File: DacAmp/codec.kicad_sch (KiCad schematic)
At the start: 0 parts

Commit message: add usb + codec
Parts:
- added C1, C8: 10u, Capacitor_SMD:C_0805_2012Metric_Pad1.18x1.45mm_HandSolder, symbol Device:C
- added C10, C9: 20p, Capacitor_SMD:C_0402_1005Metric_Pad0.74x0.62mm_HandSolder, symbol Device:C
- added C3, C4, C5: 1u, Capacitor_SMD:C_0402_1005Metric_Pad0.74x0.62mm_HandSolder, symbol Device:C
- added C6, C7: 1u, Capacitor_SMD:C_0402_1005Metric_Pad0.74x0.62mm_HandSolder, symbol Device:C_Small
- added R1: 1k5, Resistor_SMD:R_0402_1005Metric_Pad0.72x0.64mm_HandSolder, symbol Device:R_US
- added R3, R4: 22R, Resistor_SMD:R_0402_1005Metric_Pad0.72x0.64mm_HandSolder, symbol Device:R_US
- added R5, R6: 1k5, Resistor_SMD:R_0402_1005Metric_Pad0.72x0.64mm_HandSolder, symbol Device:R_Small_US
- added R7: 1M, Resistor_SMD:R_0402_1005Metric_Pad0.72x0.64mm_HandSolder, symbol Device:R_US
- added U1: PCM2906C, Package_SO:SSOP-28_5.3x10.2mm_P0.65mm, symbol Audio:PCM2902
- added Y1: 12MHz, ABM8:XTAL_ABM8-12.000MHZ-12-B1U-T, symbol Device:Crystal_GND24
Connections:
- new net 3V7: C1.1, U1.10 (VCCCI)
- new net CONN_D+: R1.2, R3.1
- new net CONN_D-: R4.1
- new net GND: C1.2, C10.2, C3.2, C4.2, C5.2, C6.2, C7.2, C8.2, C9.2, R5.2, R6.2, U1.11 (AGNDC), U1.18 (AGNDP), U1.22 (AGNDX), U1.26 (DGND), U1.4 (DGNDU), Y1.2, Y1.4
- new net HID0: U1.5 (HID0)
- new net HID1: U1.6 (HID1)
- new net HID2: U1.7 (HID2)
- new net USB_D+: R3.2, U1.1 (D+)
- new net USB_D-: R4.2, U1.2 (D-)
- new net VBUS: C6.1, U1.3 (VBUS)
- new net VCCP1I: C5.1, U1.17 (VCCP1I)
- new net VCCP2I: C4.1, U1.19 (VCCP2I)
- new net VCCXI: C3.1, U1.23 (VCCXI)
- new net VCOM: C8.1, U1.14 (VCOM)
- new net VDDI: C7.1, R1.1, U1.27 (VDDI), U1.8 (SEL0), U1.9 (SEL1)
- new net VINL: R5.1, U1.12 (VINL)
- new net VINR: R6.1, U1.13 (VINR)
- new net VOUTL: U1.16 (VOUTL)
- new net VOUTR: U1.15 (VOUTR)
- new net XTI: C10.1, R7.2, U1.21 (XTI), Y1.3
- new net XTO: C9.1, R7.1, U1.20 (XTO), Y1.1
- new net ~{SSPND}: U1.28 (~{SSPND})
- no-connect marks 0 -> 2

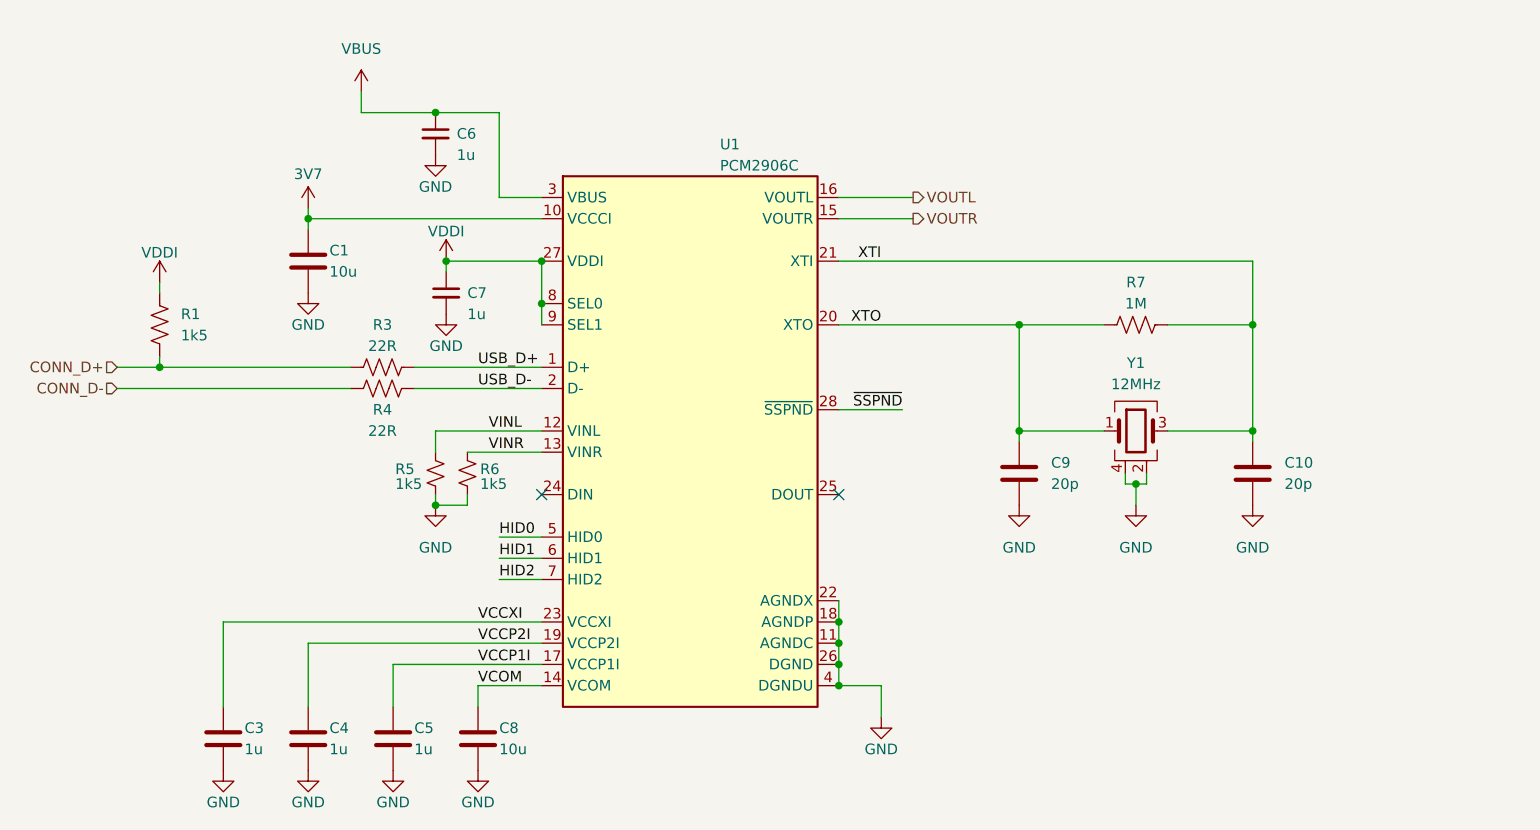
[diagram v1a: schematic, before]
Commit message: add op amps to ampR
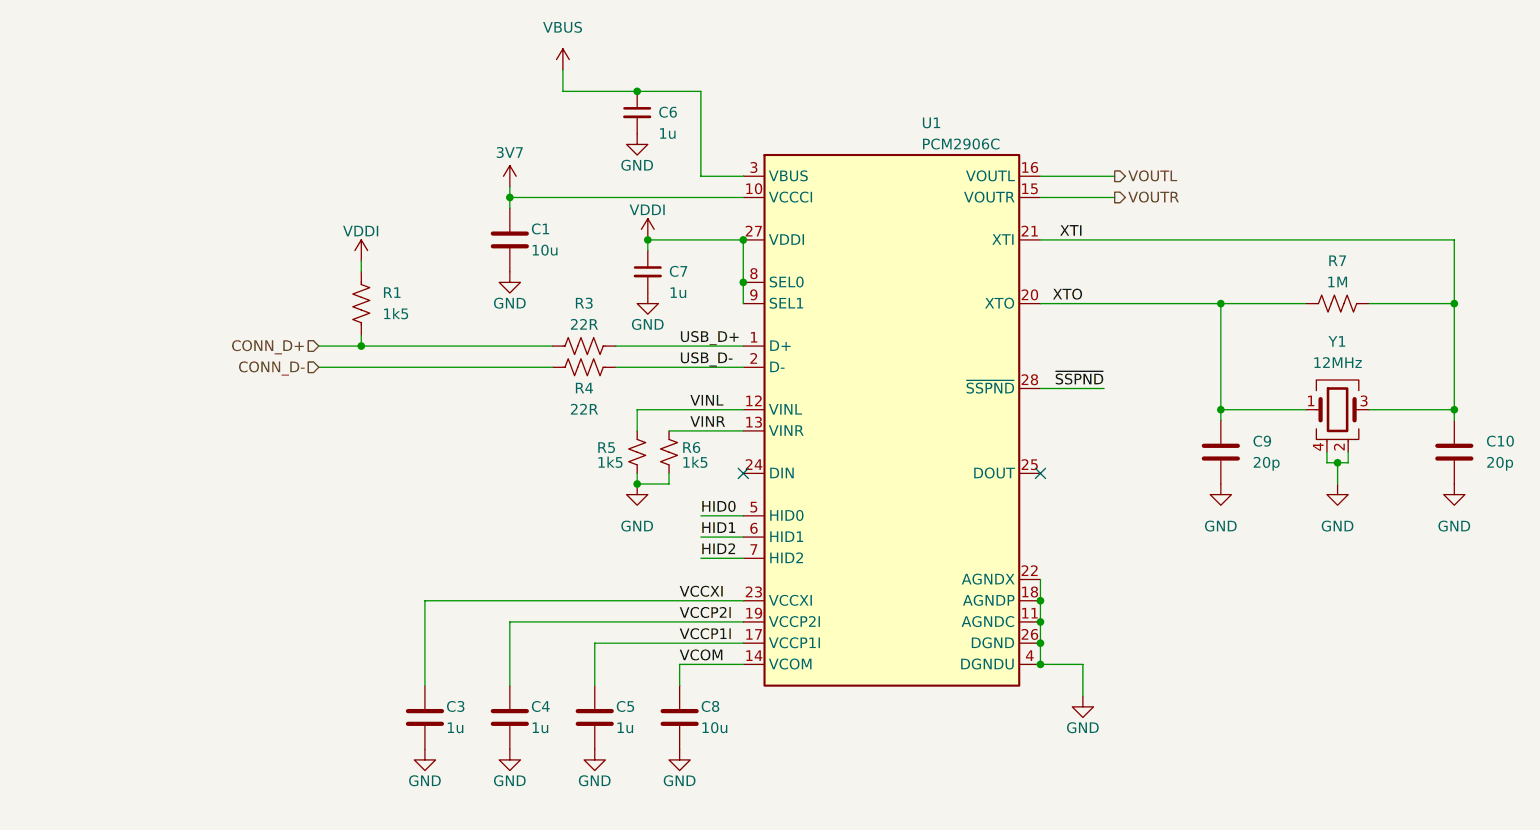
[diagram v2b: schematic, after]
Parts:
- R1: value 1k5 -> 1k5
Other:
- moved on the sheet: C1, C10, C3, C4, C5, C6, C7, C8, C9, R1, R3, R4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

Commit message: add components and footprints
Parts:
- Y1: footprint ABM8:XTAL_ABM8-12.000MHZ-12-B1U-T -> ABM8_12_000MHZ_12_B1U_T:XTAL_ABM8-12.000MHZ-12-B1U-T
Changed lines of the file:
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@@
 			)
 		)
-		(property "Footprint" "ABM8:XTAL_ABM8-12.000MHZ-12-B1U-T"
+		(property "Footprint" "ABM8_12_000MHZ_12_B1U_T:XTAL_ABM8-12.000MHZ-12-B1U-T"
 			(at 205.74 95.25 0)
 			(effects
